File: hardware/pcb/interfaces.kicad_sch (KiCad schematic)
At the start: 25 parts, among them J10 PROG, J3 132289, J8 I2C, J9 GPIO

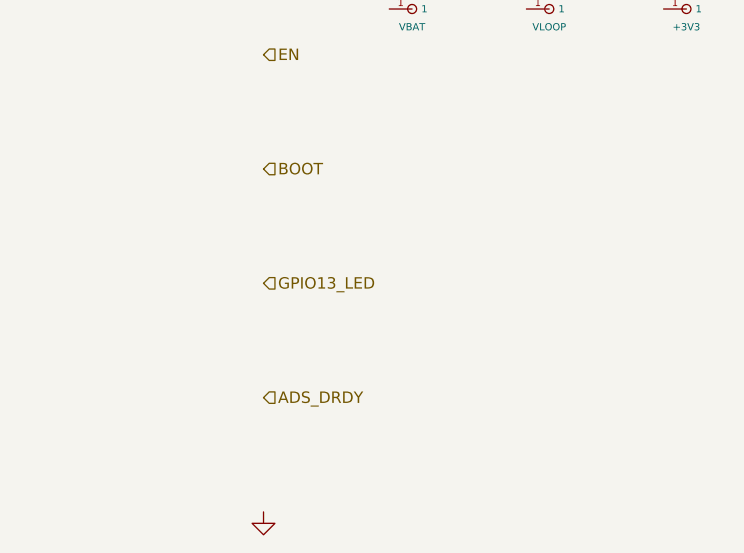
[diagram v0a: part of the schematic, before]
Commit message: hw(pcb): electrical review pass — fix 3V3 regulator variant, boost topology, GPIO13 LED conflict
Full electrical-correctness-gate review of the fresh-start design. Two of
the four CRITICALs from the 2026-05-25 senior review were resolved
incorrectly; this pass corrects them and fixes new findings:

- U1: AP63205WU is the 5 V fixed variant and the R_FBH/R_FBL values
  (560k/124k) assume a 0.6 V reference no AP6320x has — every
  combination overdrives the 3V3 rail. Swap to AP63203WU (3.3 V fixed),
  FB tied to +3V3, R_FBH/R_FBL marked DNP.
- MT3608B VLOOP: documented wiring was a buck topology and the BOM had
  no output rectifier (async boost cannot work without one). Corrected
  to VBAT→L1→SW, added D15 (SS34) and a Q3/Q4 load-disconnect so VBAT
  doesn't leak to the loop terminals through L1+D15 during deep sleep.
- Status LED moved GPIO13 → GPIO14: a green LED + 1k on GPIO13 holds
  the factory-reset strap LOW at boot → NVS wipe every boot. TP13 pad
  added for field factory reset.
- Battery divider reworked to high-side P-FET (Q5): the low-side switch
  left AIN2 biased above ADS1115 VDD through R7 (~14 uA sleep leak).
  C8 100nF → 1nF to fit the firmware's 1 ms enable window.
- TVS D8/D14 SMAJ28CA → SMAJ24CA (zero margin to CN3722 28 V abs max);
  C17 → 35 V/1206; C21 → 50 V; D6 footprint SOD-123 → SMB.
- /CHRG_SOLAR pull-up (R25), VBOOST_EN pull-down (R27), ESP32 EN RC
  (R15/C36) added; C25 duplicate bootstrap cap deleted; C16 assigned as
  U1 VIN bulk.
- schematic_connections.md rewritten pin-name-based with a symbol
  pin-number verification table and datasheet-verification blocker list;
  BOM/placement/guide/placement-script reconciled (phantom refdes,
  wrong ADS1115 pin numbers, mis-documented MPPT divider, shunt return
  path contradiction).

Flagged, not fixed: TP5100 cannot charge 2S from 5 V USB (step-down
charger) — needs an IC swap; schematic still has zero drawn wires; five
IC symbol pinouts pending datasheet verification before ordering.

Co-Auth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
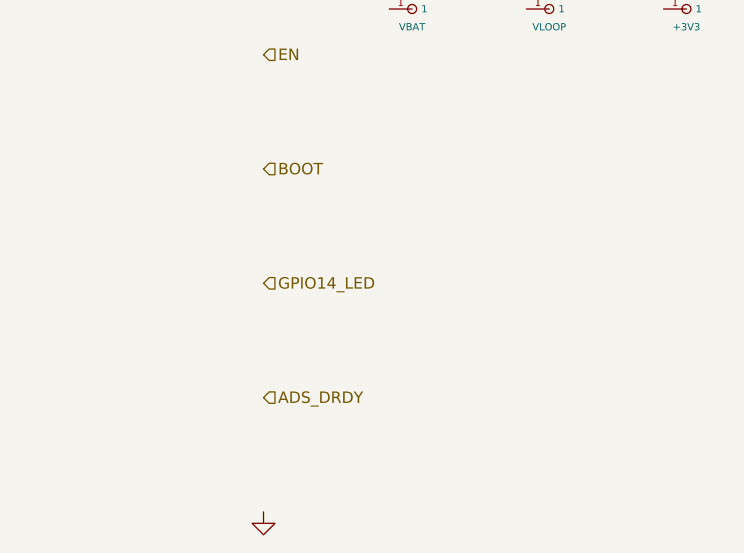
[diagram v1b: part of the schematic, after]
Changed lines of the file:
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@@
 		(company "WellD Project")
 	)
-	(hierarchical_label "GPIO13_LED"
+	(hierarchical_label "GPIO14_LED"
 		(shape input)
 		(at 25.4 165.1 0)

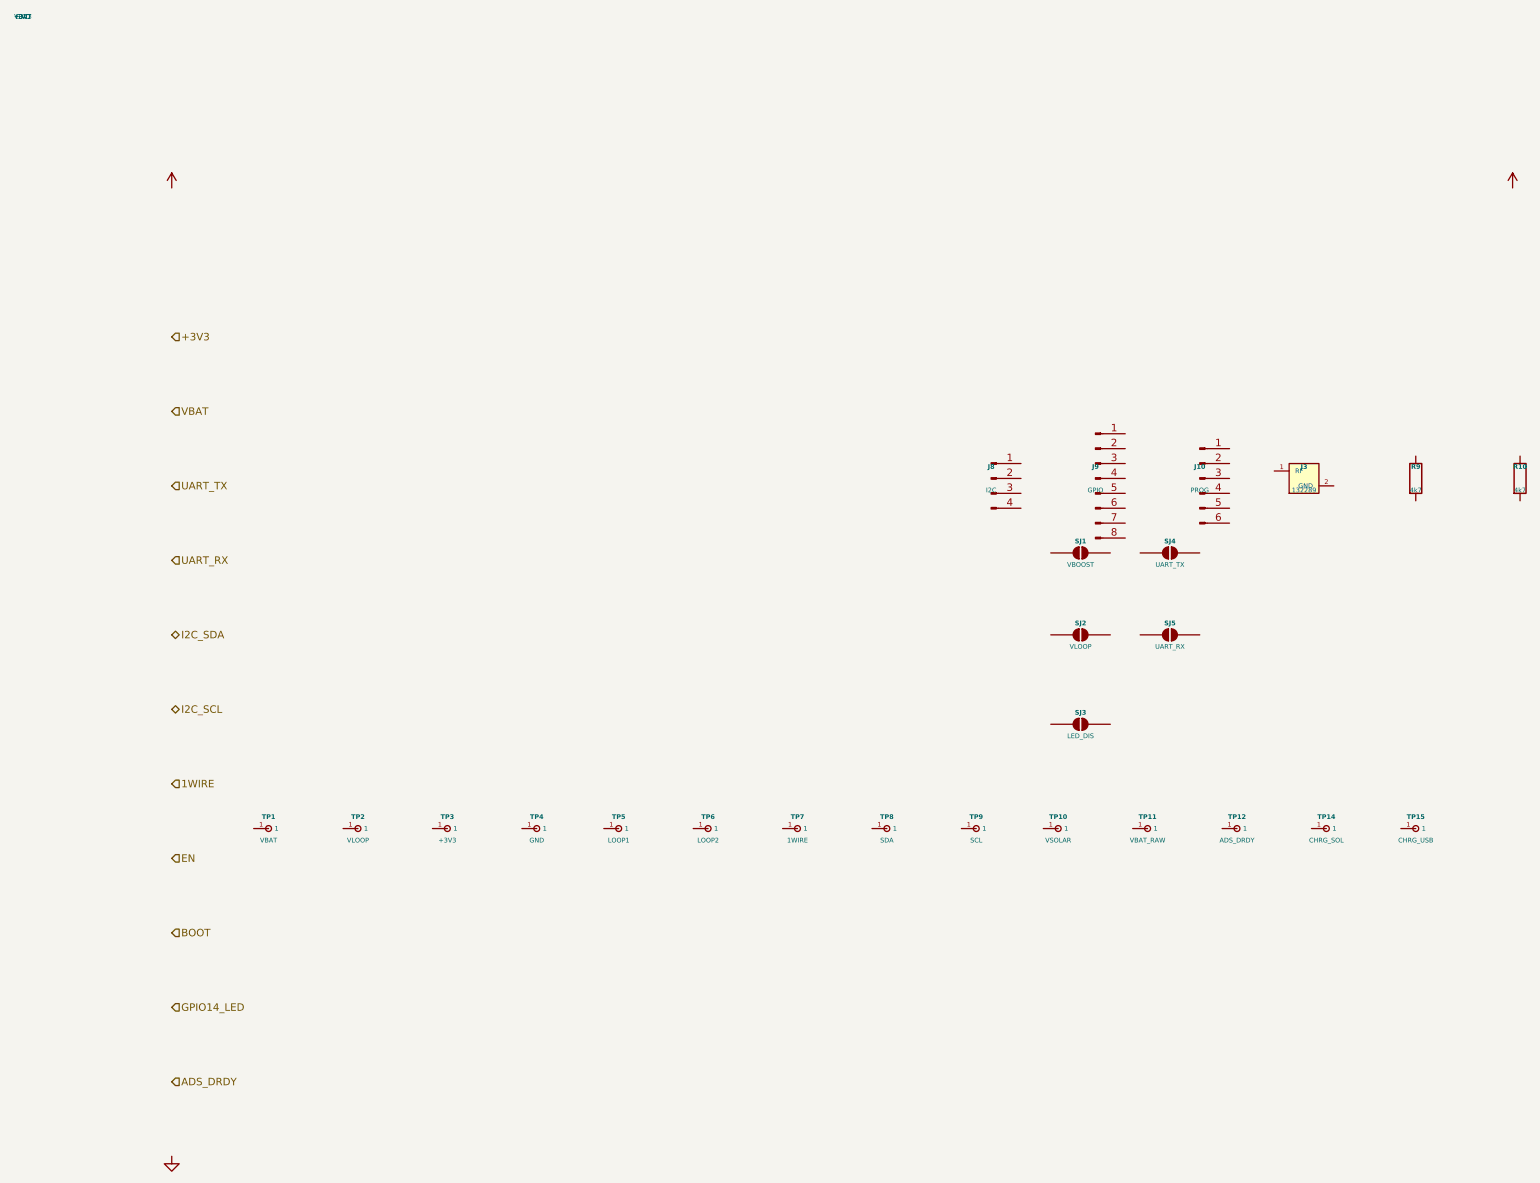
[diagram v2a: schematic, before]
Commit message: hw(pcb): wiring pass — schematic fully wired, netlist machine-verified (0 mismatches)
All four sheets wired with stub+label connectivity (434 wires, 21
explicit no-connects, PWR_FLAGs on undriven rails): power rails on
global labels, cross-sheet signals on hierarchical labels + rebuilt
top-sheet pins (24 hierarchical nets; vestigial ADC_CH* pins deleted,
GPIO14_LED corrected to the mcu-local net it really is), sheet-local
nets on local labels.

Verification (kicad-cli for the KiCad-10 format is not installable
here): hardware/pcb/kicad_wire_script.py generates the connectivity
from an embedded intent table derived from schematic_connections.md;
hardware/pcb/netlist_check.py independently re-extracts pin->net
geometrically (union-find over wires/labels/sheet pins) and diffs —
395 pins, 77 nets, 0 mismatches (output committed). Native KiCad 10
ERC + resave queued for the first interactive open.

Notable resolutions (recorded as design change #17): AP63203 FB tied
to +3V3 with the DNP divider floated at its midpoint; MT3608B pin 6
etype relaxed to passive so C_BST wiring is ERC-legal; IP2326 DM/DP
floated with no-connects (adapter detection is a two-wire future
change); D11 oriented cathode-to-VLOOP; decorative corner power
symbols replaced with real rail connectivity.

placement_constraints.md: Group G rewritten for the IP2326 hot loop,
new Group L for the CN3722 external buck (Kelvin CSP/BAT pair).
Top remaining risk flagged in blockers: AP63203 BST is NC per the
wiring doc but the AP6320x family likely requires a BST-SW cap —
resolve before layout freeze.

Co-Authored-By: Claude Fable 5 <noreply@anthropic.com>
Claude-Session: https://claude.ai/code/session_01VtMFY5Q94iYbsNPpLcPJyK
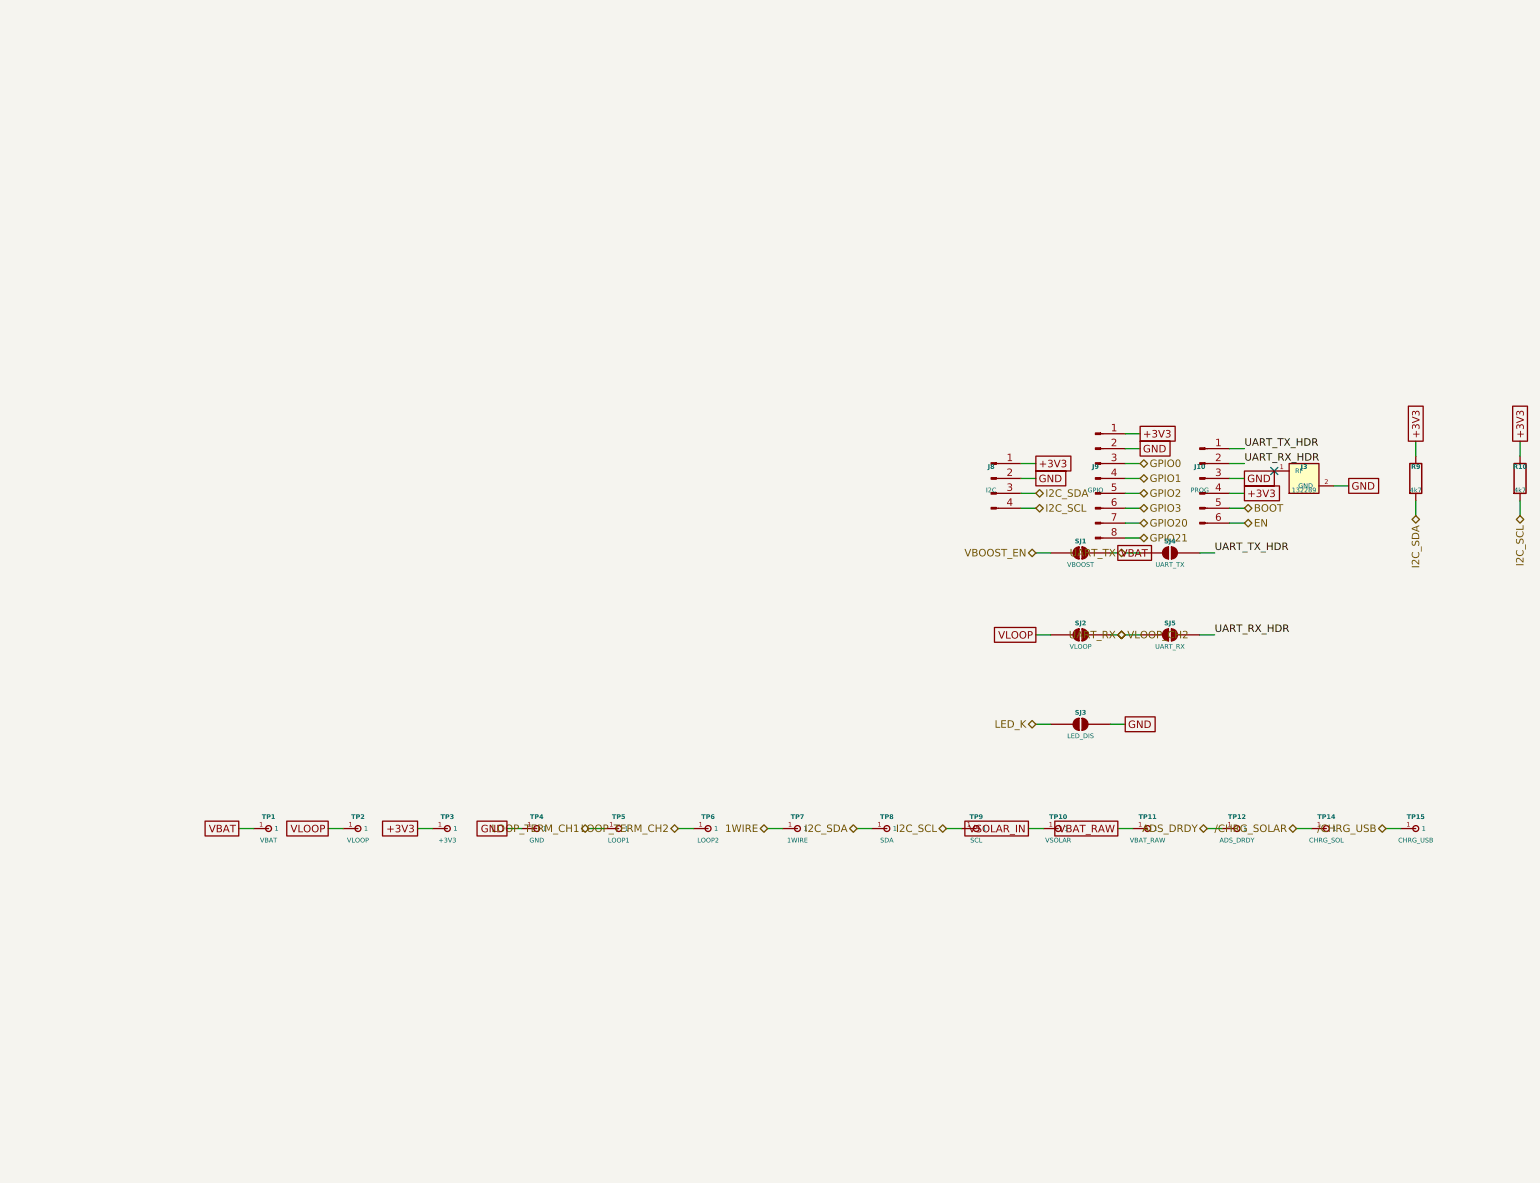
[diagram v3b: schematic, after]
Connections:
- net +3V3: now also J10.4 (Pin_4), J8.1 (Pin_1), J9.1 (Pin_1), R10.1, R9.1, TP3.1
- net 1WIRE: now also TP7.1
- net ADS_DRDY: now also TP12.1
- net BOOT: now also J10.5 (Pin_5)
- net EN: now also J10.6 (Pin_6)
- net GND: now also J10.3 (Pin_3), J3.2 (GND), J8.2 (Pin_2), J9.2 (Pin_2), SJ3.2 (B), TP4.1
- net I2C_SCL: now also J8.4 (Pin_4), R10.2, TP9.1
- net I2C_SDA: now also J8.3 (Pin_3), R9.2, TP8.1
- net UART_RX: now also SJ5.1 (A)
- net UART_TX: now also SJ4.1 (A)
- net VBAT: now also SJ1.2 (B), TP1.1
- net VSOLAR_IN: now reaches TP10.1
- net UART_RX_HDR: now reaches SJ5.2 (B)
- net UART_RX_HDR: now also J10.2 (Pin_2)
- net UART_TX_HDR: now reaches SJ4.2 (B)
- net UART_TX_HDR: now also J10.1 (Pin_1)
- net VLOOP: now reaches TP2.1
- net VLOOP: now also SJ2.1 (A)
- net VBAT_RAW: now reaches TP11.1
- net VBOOST_EN: now reaches SJ1.1 (A)
- net /CHRG_SOLAR: now reaches TP14.1
- net /CHRG_USB: now reaches TP15.1
- net VLOOP_CH2: now reaches SJ2.2 (B)
- net LED_K: now reaches SJ3.1 (A)
- net LOOP_TERM_CH2: now reaches TP6.1
- net LOOP_TERM_CH1: now reaches TP5.1
- net GPIO0: now reaches J9.3 (Pin_3)
- net GPIO1: now reaches J9.4 (Pin_4)
- net GPIO2: now reaches J9.5 (Pin_5)
- net GPIO3: now reaches J9.6 (Pin_6)
- net GPIO20: now reaches J9.7 (Pin_7)
- net GPIO21: now reaches J9.8 (Pin_8)
- no-connect marks 0 -> 1
